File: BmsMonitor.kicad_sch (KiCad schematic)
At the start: 9 parts, among them J1 Conn_01x03, J2 Conn_01x03, J3 Conn_01x04, J4 Conn_01x22, J5 Conn_01x22, U1 2365-DC-DC module, U2 ESP32-S3-DevKitC, U3 TJA1050 Module, U4 Open-Smart_3.8_LCD

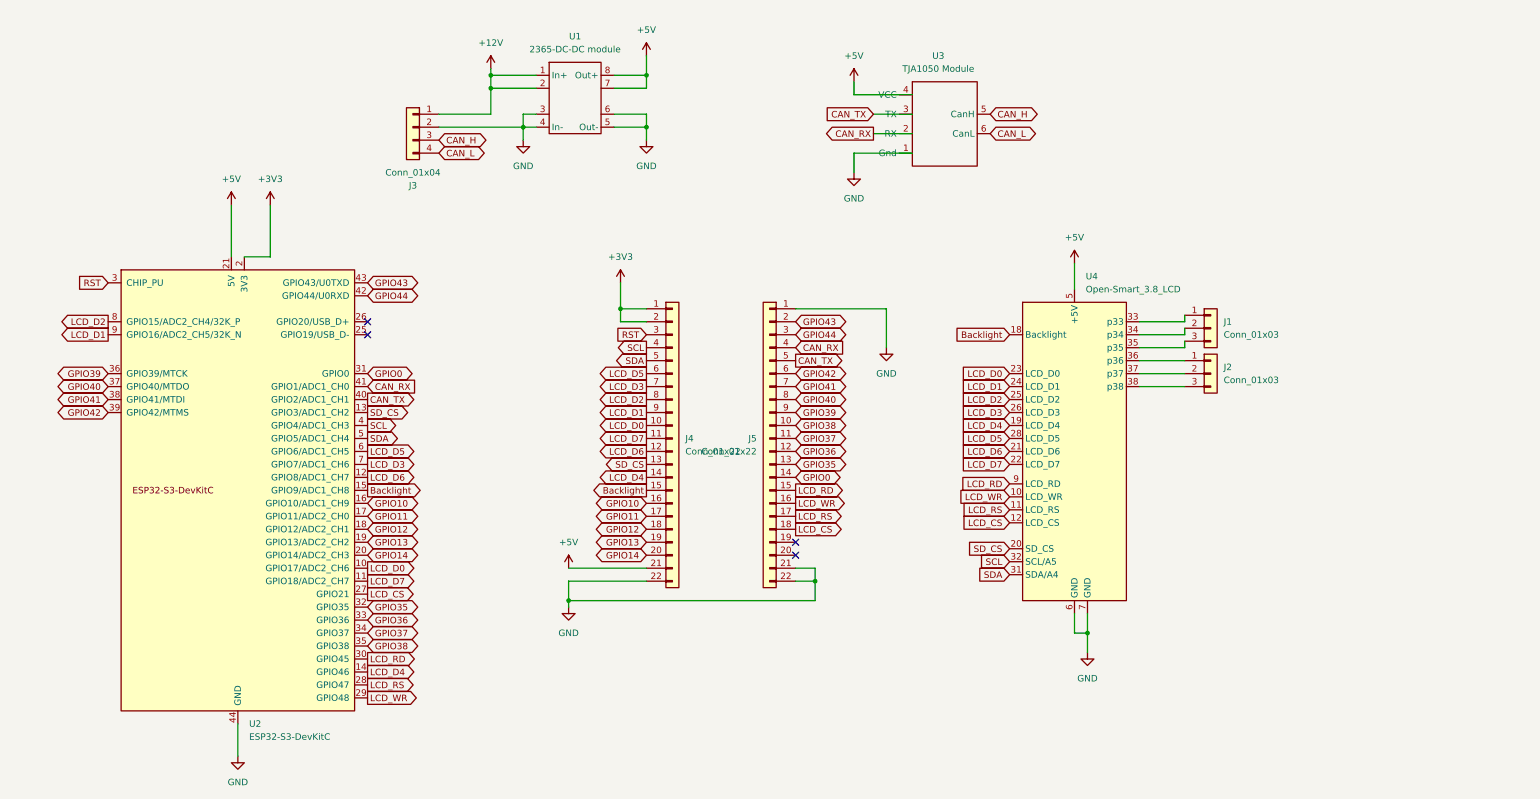
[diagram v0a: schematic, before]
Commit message: BmsMonitor Ver 2.0
Changed to work with Display having a SPI variant of ILI9488
as well as a XPT2046 touch controller.

The display in question is this 3.5" display:
https://www.aliexpress.com/item/33057812377.html
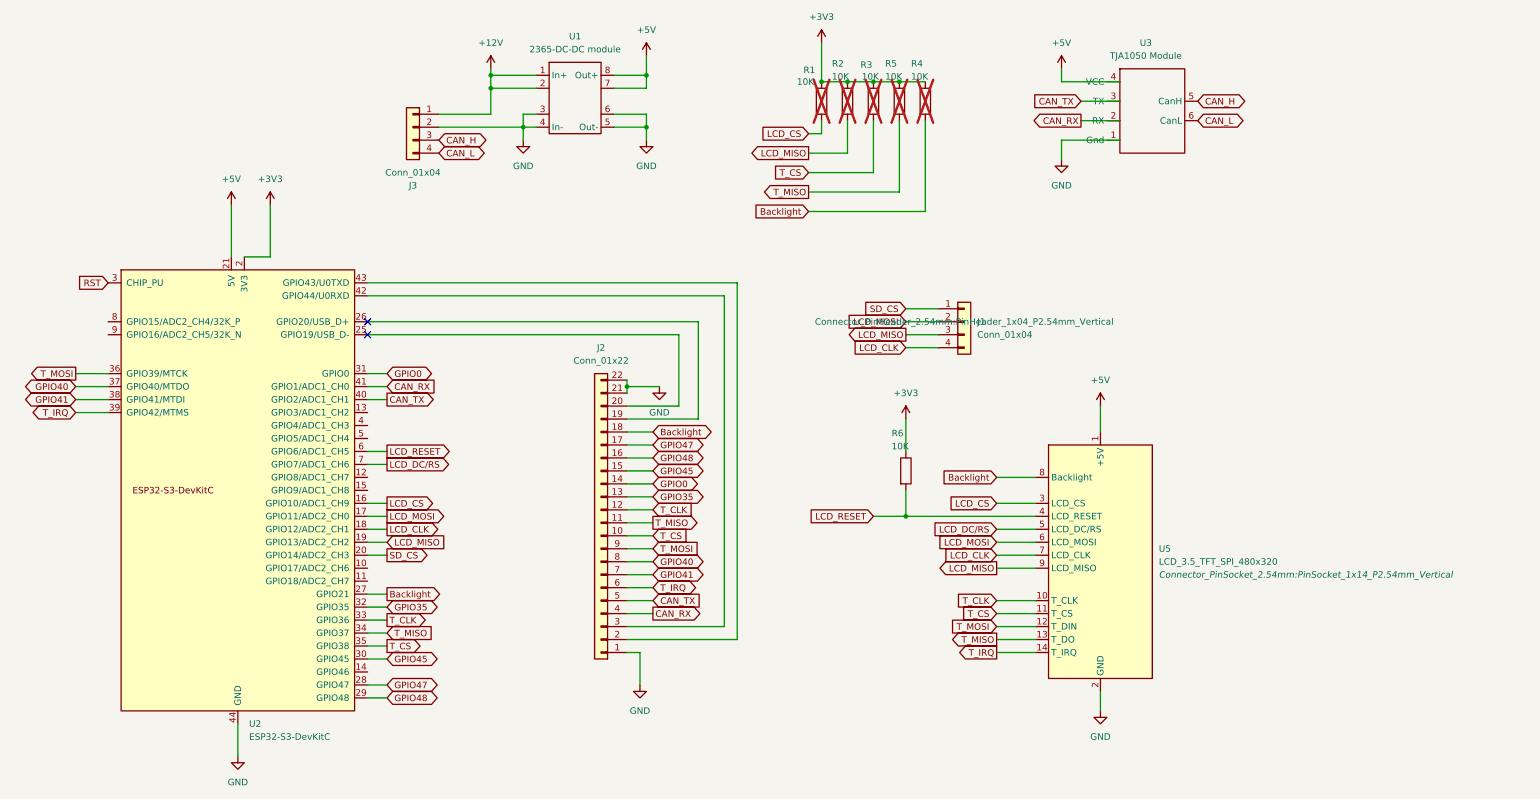
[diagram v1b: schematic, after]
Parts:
- removed J1, J2: Conn_01x03, Connector_PinHeader_2.54mm:PinHeader_1x03_P2.54mm_Vertical, symbol Connector_Generic:Conn_01x03
- removed J4, J5: Conn_01x22, Connector_PinSocket_2.54mm:PinSocket_1x22_P2.54mm_Vertical, symbol Connector_Generic:Conn_01x22
- removed U4: Open-Smart_3.8_LCD, Private:Open_smart_3.8_LCD, symbol Private:Open-Smart_3.8_LCD
- added J1: Conn_01x04, Connector_PinHeader_2.54mm:PinHeader_1x04_P2.54mm_Vertical, symbol Connector_Generic:Conn_01x04
- added J2: Conn_01x22, Connector_PinHeader_2.54mm:PinHeader_1x22_P2.54mm_Vertical, symbol Connector_Generic:Conn_01x22
- added R1, R2, R3, R4, R5, R6: 10K, Resistor_THT:R_Box_L8.4mm_W2.5mm_P5.08mm, symbol Device:R
- added U5: LCD_3.5_TFT_SPI_480x320, Connector_PinSocket_2.54mm:PinSocket_1x14_P2.54mm_Vertical, symbol Private:LCD_3.5_TFT_SPI_480x320
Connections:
- net GPIO10 is gone; now on net LCD_CS: U2.16 (GPIO10/ADC1_CH9)
- net GPIO14 is gone; now on net SD_CS: U2.20 (GPIO14/ADC2_CH3)
- net +3V3: now also R1.1, R2.1, R3.1, R4.1, R5.1, R6.1
- net +5V: now also U5.1 (+5V)
- net Backlight: now also U2.27 (GPIO21), J2.18 (Pin_18), R4.2, U5.8 (Backlight); no longer U2.15 (GPIO9/ADC1_CH8)
- net CAN_RX: now also J2.4 (Pin_4)
- net CAN_TX: now also J2.5 (Pin_5)
- net GND: now also J2.1 (Pin_1), J2.21 (Pin_21), J2.22 (Pin_22), U5.2 (GND)
- net GPIO0: now also J2.14 (Pin_14)
- net GPIO35: now also J2.13 (Pin_13)
- net GPIO40: now also J2.8 (Pin_8)
- net GPIO41: now also J2.7 (Pin_7)
- net LCD_CS: now also R1.2, U5.3 (LCD_CS); no longer U2.27 (GPIO21)
- net SD_CS: now also J1.1 (Pin_1); no longer U2.13 (GPIO3/ADC1_CH2)
- net at U2.25 (GPIO19/USB_D-): now also J2.20 (Pin_20)
- net at U2.26 (GPIO20/USB_D+): now also J2.19 (Pin_19)
- net GPIO11 renamed LCD_MOSI
- net LCD_MOSI: now also J1.2 (Pin_2), U5.6 (LCD_MOSI)
- net GPIO12 renamed LCD_CLK
- net LCD_CLK: now also J1.4 (Pin_4), U5.7 (LCD_CLK)
- net GPIO13 renamed LCD_MISO
- net LCD_MISO: now also J1.3 (Pin_3), R2.2, U5.9 (LCD_MISO)
- net GPIO36 renamed T_CLK
- net T_CLK: now also J2.12 (Pin_12), U5.10 (T_CLK)
- net GPIO37 renamed T_MISO
- net T_MISO: now also J2.11 (Pin_11), R5.2, U5.13 (T_DO)
- net GPIO38 renamed T_CS
- net T_CS: now also J2.10 (Pin_10), R3.2, U5.11 (T_CS)
- net GPIO39 renamed T_MOSI
- net T_MOSI: now also J2.9 (Pin_9), U5.12 (T_DIN)
- net GPIO42 renamed T_IRQ
- net T_IRQ: now also J2.6 (Pin_6), U5.14 (T_IRQ)
- net GPIO43: no longer names the net of U2.43 (GPIO43/U0TXD)
- net GPIO43: now also J2.2 (Pin_2)
- net GPIO44: no longer names the net of U2.42 (GPIO44/U0RXD)
- net GPIO44: now also J2.3 (Pin_3)
- net LCD_D0: no longer names the net of U2.10 (GPIO17/ADC2_CH6)
- net LCD_D1: no longer names the net of U2.9 (GPIO16/ADC2_CH5/32K_N)
- net LCD_D2: no longer names the net of U2.8 (GPIO15/ADC2_CH4/32K_P)
- net LCD_D3 renamed LCD_DC/RS
- net LCD_DC/RS: now also U5.5 (LCD_DC/RS)
- net LCD_D4: no longer names the net of U2.14 (GPIO46)
- net LCD_D5 renamed LCD_RESET
- net LCD_RESET: now also R6.2, U5.4 (LCD_RESET)
- net LCD_D6: no longer names the net of U2.12 (GPIO8/ADC1_CH7)
- net LCD_D7: no longer names the net of U2.11 (GPIO18/ADC2_CH7)
- net LCD_RD renamed GPIO45
- net GPIO45: now also J2.15 (Pin_15)
- net LCD_RS renamed GPIO47
- net GPIO47: now also J2.17 (Pin_17)
- net LCD_WR renamed GPIO48
- net GPIO48: now also J2.16 (Pin_16)
- net SCL: no longer names the net of U2.4 (GPIO4/ADC1_CH3)
- net SDA: no longer names the net of U2.5 (GPIO5/ADC1_CH4)
- no-connect marks 4 -> 2
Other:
- moved on the sheet: U3

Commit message: Use common SPI for both display and touch.
Added M12 connector for possible power and CAN
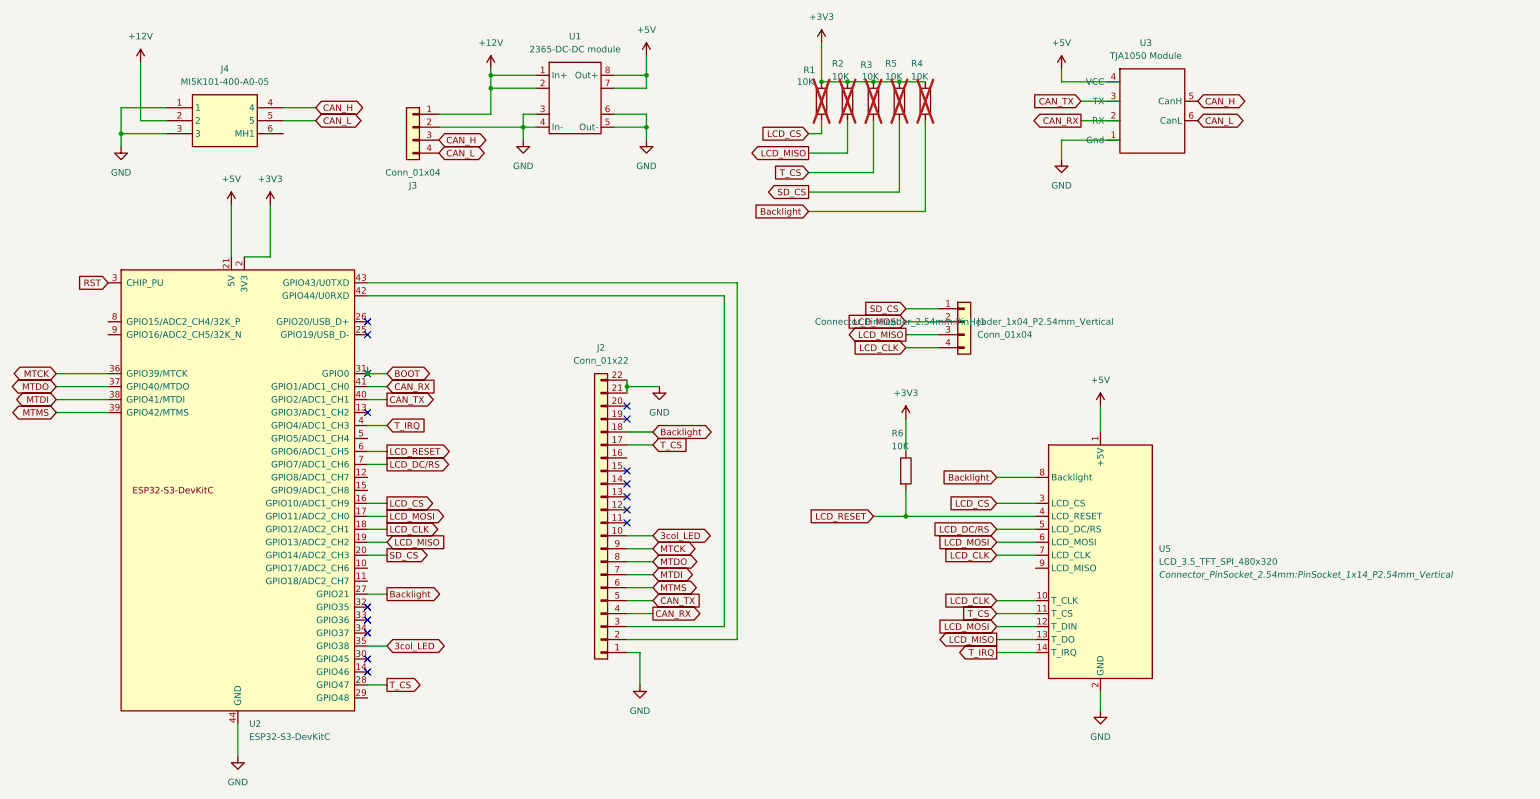
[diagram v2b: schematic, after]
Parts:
- added J4: MI5K101-400-A0-05, MI5K101400A005, symbol M12 NMEA2000:MI5K101-400-A0-05
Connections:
- net GPIO47 is gone; now on net T_CS: J2.17 (Pin_17), U2.28 (GPIO47)
- net +12V: now also J4.2
- net CAN_H: now also J4.4
- net CAN_L: now also J4.5
- net GND: now also J4.1, J4.3
- net LCD_CLK: now also U5.10 (T_CLK)
- net LCD_MISO: now also U5.13 (T_DO); no longer U5.9 (LCD_MISO)
- net LCD_MOSI: now also U5.12 (T_DIN)
- net SD_CS: now also R5.2
- net T_CS: no longer J2.10 (Pin_10), U2.35 (GPIO38)
- net T_IRQ: now also U2.4 (GPIO4/ADC1_CH3); no longer J2.6 (Pin_6), U2.39 (GPIO42/MTMS)
- net at U2.25 (GPIO19/USB_D-): no longer J2.20 (Pin_20)
- net at U2.26 (GPIO20/USB_D+): no longer J2.19 (Pin_19)
- net GPIO0: no longer names the net of J2.14 (Pin_14)
- net GPIO0: no longer U2.31 (GPIO0)
- net GPIO35: no longer names the net of U2.32 (GPIO35)
- net GPIO35: no longer J2.13 (Pin_13)
- net GPIO40 renamed MTDO
- net GPIO41 renamed MTDI
- net GPIO45: no longer names the net of U2.30 (GPIO45)
- net GPIO45: no longer J2.15 (Pin_15)
- net GPIO48: no longer names the net of U2.29 (GPIO48)
- net GPIO48: no longer J2.16 (Pin_16)
- removed net T_CLK: J2.12 (Pin_12), U2.33 (GPIO36), U5.10 (T_CLK)
- removed net T_MISO: J2.11 (Pin_11), R5.2, U2.34 (GPIO37), U5.13 (T_DO)
- net T_MOSI renamed MTCK
- net MTCK: no longer U5.12 (T_DIN)
- new net 3col_LED: J2.10 (Pin_10), U2.35 (GPIO38)
- new net BOOT: U2.31 (GPIO0)
- new net MTMS: J2.6 (Pin_6), U2.39 (GPIO42/MTMS)
- no-connect marks 2 -> 16
